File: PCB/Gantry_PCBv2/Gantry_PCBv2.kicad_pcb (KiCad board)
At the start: 2 copper layers, 190.5 x 121.8 mm, 169 parts, among them J1 Screw_Terminal_01x02, J10 B2B-XH-A_LF__SN_, J11 USB_C_Receptacle_USB2.0_16P, J12 Conn_01x04_Pin, J13 Conn_01x04_Pin, J14 Conn_01x04_Pin, J15 Conn_01x04_Pin, J16 Conn_01x05_Pin, J17 Conn_01x05_Pin, J2 DCJ200-10-A-XX-X_REVA, J3 Conn_01x03_Pin, J4 Conn_01x14, J5 B2B-XH-A_LF__SN_, J6 B2B-XH-A_LF__SN_, J7 B2B-XH-A_LF__SN_, J8 Conn_01x14, J9 Conn_01x10, Q1 NMOS, Q2 SS8050, Q3 SS8050, SW1 SW_0, SW2 SW_EN, SW3 SW_Push_DPDT, SW4 SW_Push_DPDT, SW5 SW_Push_DPDT, SW6 SW_Push_DPDT, U10 74HC245, U11 74HC245, U12 MCP23017_SO, U13 CP2102N-Axx-xQFN28, U14 ESP32-WROOM-32U, U2 MP1584, U4 TLV75733PDBV, U5 DRV8825_STEPPER_MOTOR_DRIVER_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, U6 DRV8825_STEPPER_MOTOR_DRIVER_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, U7 TB6612FNG H-bridge Motor Driv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, U8 DRV8825_STEPPER_MOTOR_DRIVER_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, U9 DRV8825_STEPPER_MOTOR_DRIVER_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

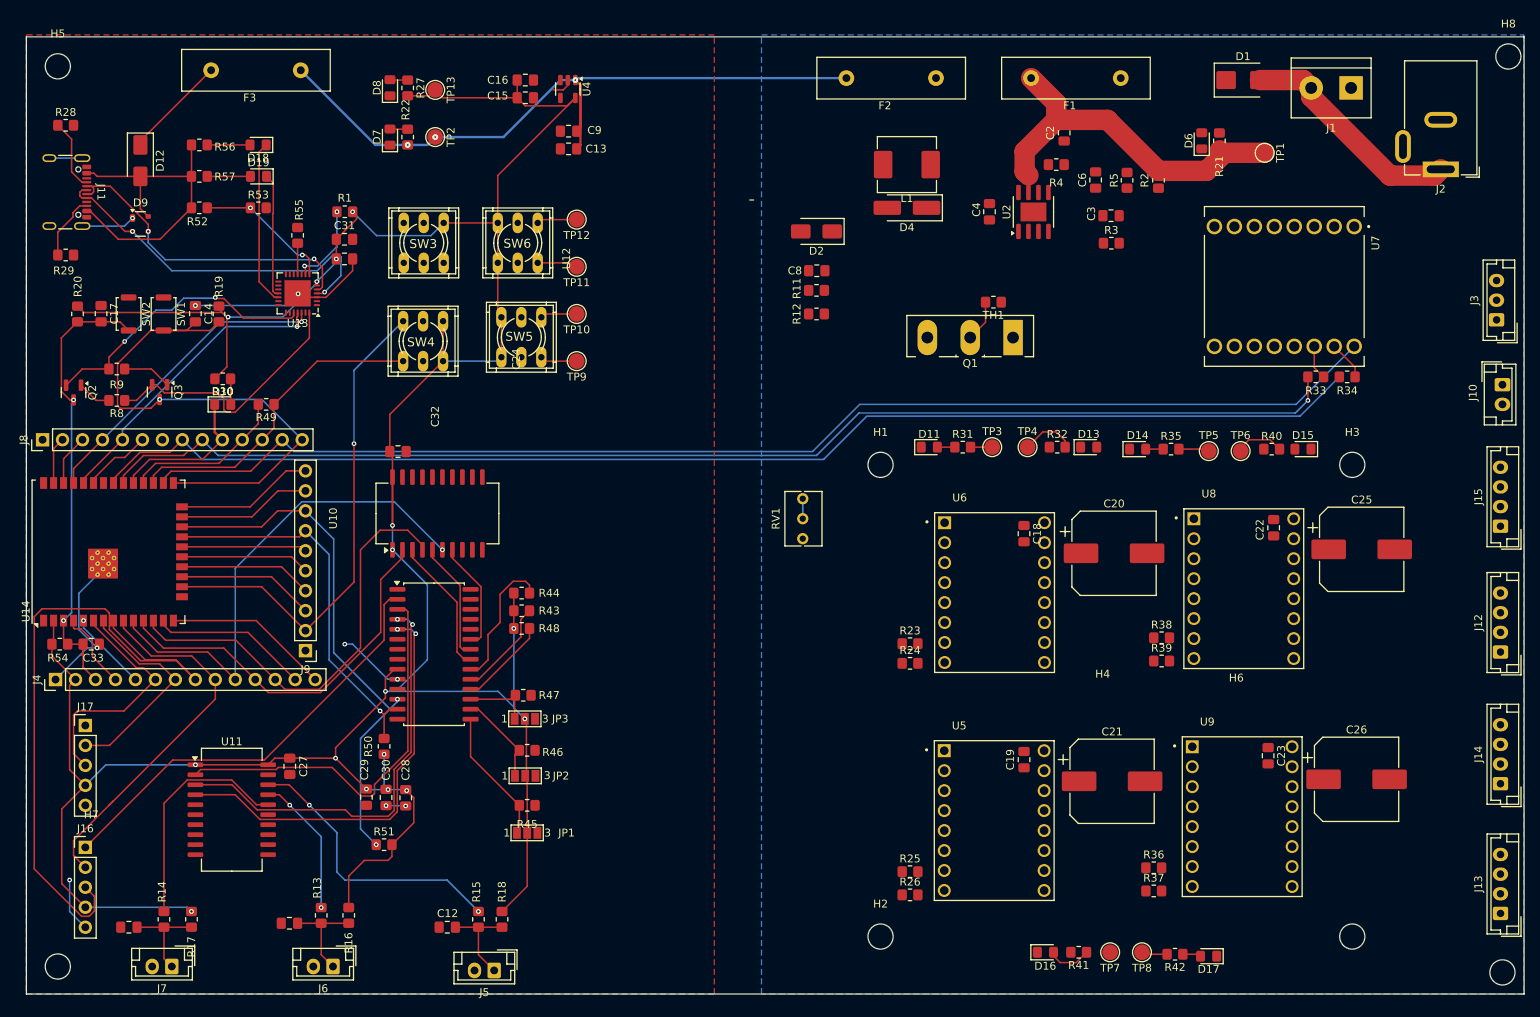
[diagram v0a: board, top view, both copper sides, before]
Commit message: PCB routing70% done
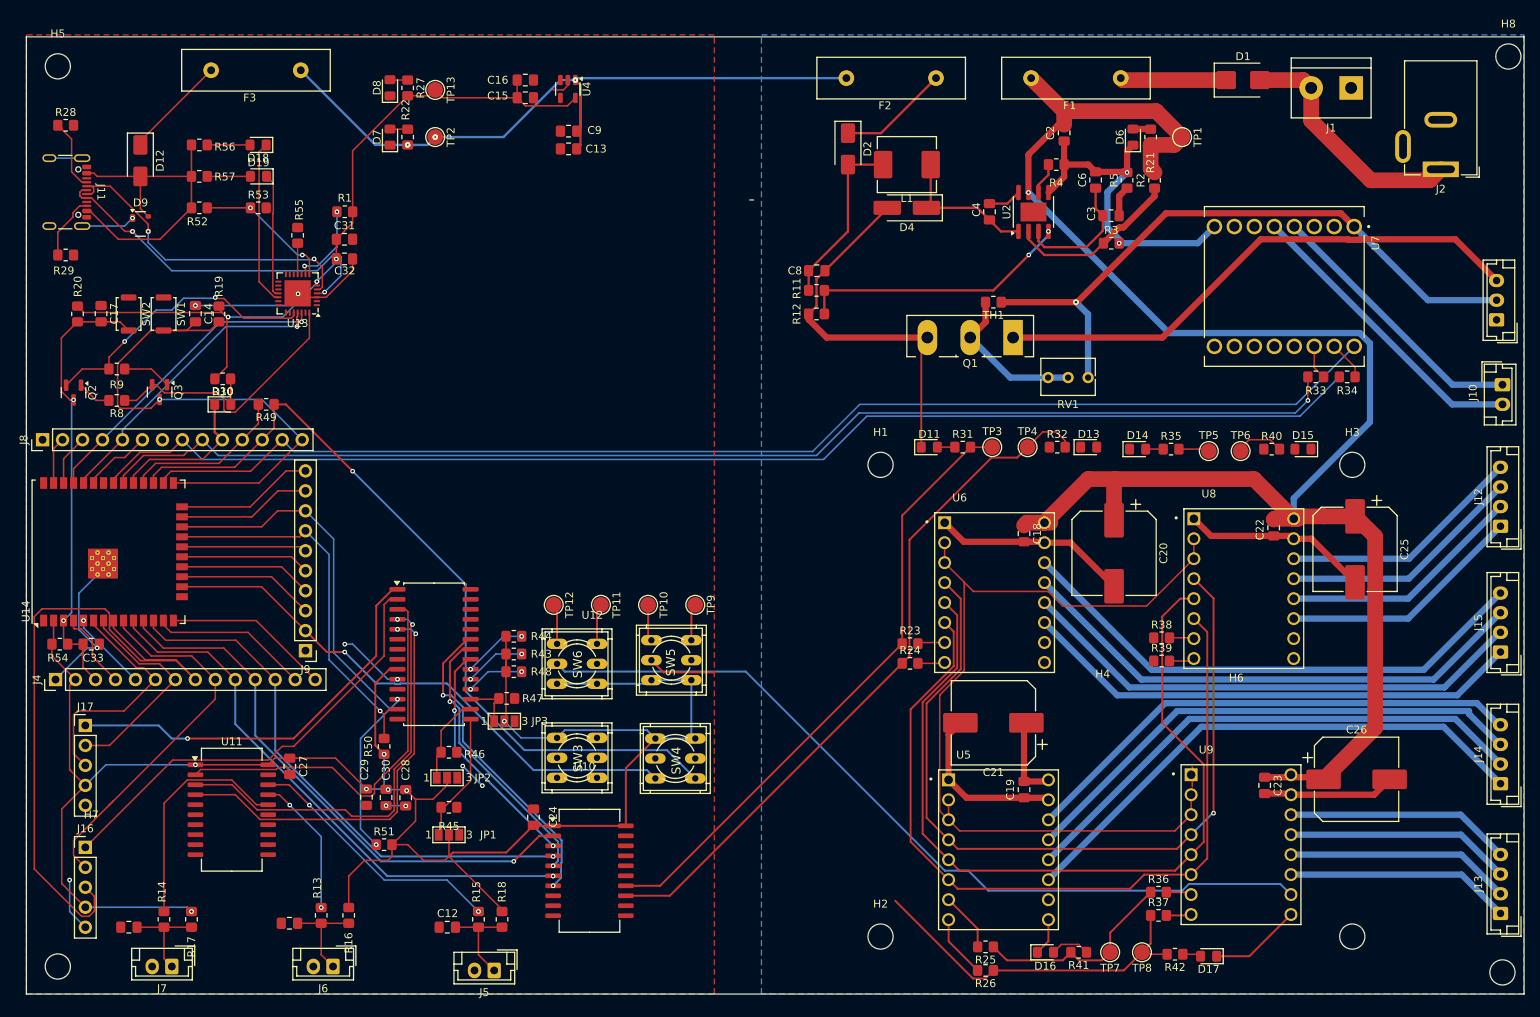
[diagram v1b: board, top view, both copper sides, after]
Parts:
- moved SW3 68.3 mm to (121.3, 115.5), turned to -90 degrees
- moved SW4 62.0 mm to (133.8, 115.5), turned to -90 degrees
- moved SW6 54.1 mm to (121.3, 103.5), turned to -90 degrees
- moved C24 49.6 mm to (115.8, 123.0), turned to -90 degrees
- moved U10 49.4 mm to (122.9, 129.8), turned to 0 degrees
- moved TP12 49.1 mm to (118.3, 96.0), turned to -90 degrees
- moved SW5 45.3 mm to (133.3, 103.0), turned to -90 degrees
- moved TP11 43.1 mm to (124.3, 96.0), turned to -90 degrees
- moved TP10 38.1 mm to (130.3, 96.0), turned to -90 degrees
- moved RV1 34.8 mm to (181.2, 67.1), turned to 180 degrees
- moved TP9 34.5 mm to (136.3, 96.0), turned to -90 degrees
- moved C21 16.8 mm to (174.2, 111.0), turned to 180 degrees
- moved J12 16.0 mm to (238.8, 86.0)
- moved J15 16.0 mm to (238.8, 102.0)
- moved R26 13.6 mm to (173.2, 142.5), turned to 180 degrees
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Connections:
- J12 pad 1: /SM2_A1 -> /SM2_A2
- J12 pad 2: /SM2_A2 -> /SM2_A1
- J13 pad 1: /SM3_A1 -> /SM3_A2
- J13 pad 2: /SM3_A2 -> /SM3_A1
- J14 pad 1: /SM4_A1 -> /SM4_A2
- J14 pad 2: /SM4_A2 -> /SM4_A1
- J15 pad 1: /SM1_A1 -> /SM1_A2
- J15 pad 2: /SM1_A2 -> /SM1_A1
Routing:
- net GND: track 74.0 -> 275.7 mm, vias 9 -> 13
- net /12V_R: track 46.3 -> 231.8 mm, vias 0 -> 1
- net /RST/PDN: track 0.00 -> 106.9 mm
- net /FLT/VIO4: track 0.00 -> 106.2 mm
- net /SLP/CLK: track 0.00 -> 103.6 mm
- net /M2/NC: track 0.00 -> 103.4 mm, vias 0 -> 1
- net /M1_D: track 6.86 -> 90.3 mm
- net /12V_P: track 0.00 -> 82.5 mm, vias 0 -> 1
- net /M1_S: track 3.21 -> 79.7 mm
- net /3V3: track 404.7 -> 474.1 mm, vias 16 -> 10
- net Net-(J3-Pin_3): track 0.00 -> 68.9 mm
- net /SM4_A2: track 0.00 -> 68.6 mm
- net /SM1_B2: track 0.00 -> 67.7 mm
- net /SM4_A1: track 0.00 -> 67.3 mm
- net /SM1_B1: track 0.00 -> 66.6 mm
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
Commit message: PCB routing 1st draft
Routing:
- net /3V3: track 474.1 -> 626.2 mm, vias 10 -> 12
- net /M2_S: track 3.90 -> 117.0 mm, vias 0 -> 4
- net /M2_D: track 6.27 -> 117.7 mm, vias 0 -> 3
- net /FLT/VIO2: track 9.43 -> 90.9 mm, vias 0 -> 1
- net /FLT/VIO3: track 0.00 -> 72.8 mm, vias 0 -> 1
- net /M2/NC: track 103.4 -> 166.2 mm, vias 1 -> 2
- net GND: track 275.7 -> 332.4 mm, vias 13 -> 14
- net /M3/4_S: track 26.6 -> 77.6 mm, vias 0 -> 2
- net /FLT/VIO1: track 0.00 -> 46.9 mm, vias 0 -> 2
- net /SLP/CLK: track 103.6 -> 150.5 mm, vias 0 -> 1
- net /RST/PDN: track 106.9 -> 145.4 mm, vias 0 -> 1
- net /32: track 85.9 -> 50.8 mm
- net /M3/4_D: track 45.3 -> 80.0 mm, vias 0 -> 2
- net /12V_R: track 231.8 -> 258.2 mm, vias 1 -> 2
- net Net-(D13-A): track 0.00 -> 6.85 mm
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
